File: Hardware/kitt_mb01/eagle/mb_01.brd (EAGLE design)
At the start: 160 x 100 mm, 120 parts, among them IC2.00 BQ24266RGET, IC3.01 LSM9DS1, U1.01 RT8293A, U6.01 TPS61032RSARPSDO-G16, U7.01 SI1922EDH, U7.03 SI1922EDH, U7.2 SI1922EDH, X2.01 S2B-PH-K-S(LF)(SN), X7.02 ARDUINO_UNO, X7.03 CON_HEADER_1X02, X7.05 MOTOR, X7.06 CON_HEADER_1X02, X7.08 CON_HEADER_1X02, X7.09 0R-JUMPA, X7.10 0R-JUMPA, X7.11 CON_HEADER_1X02

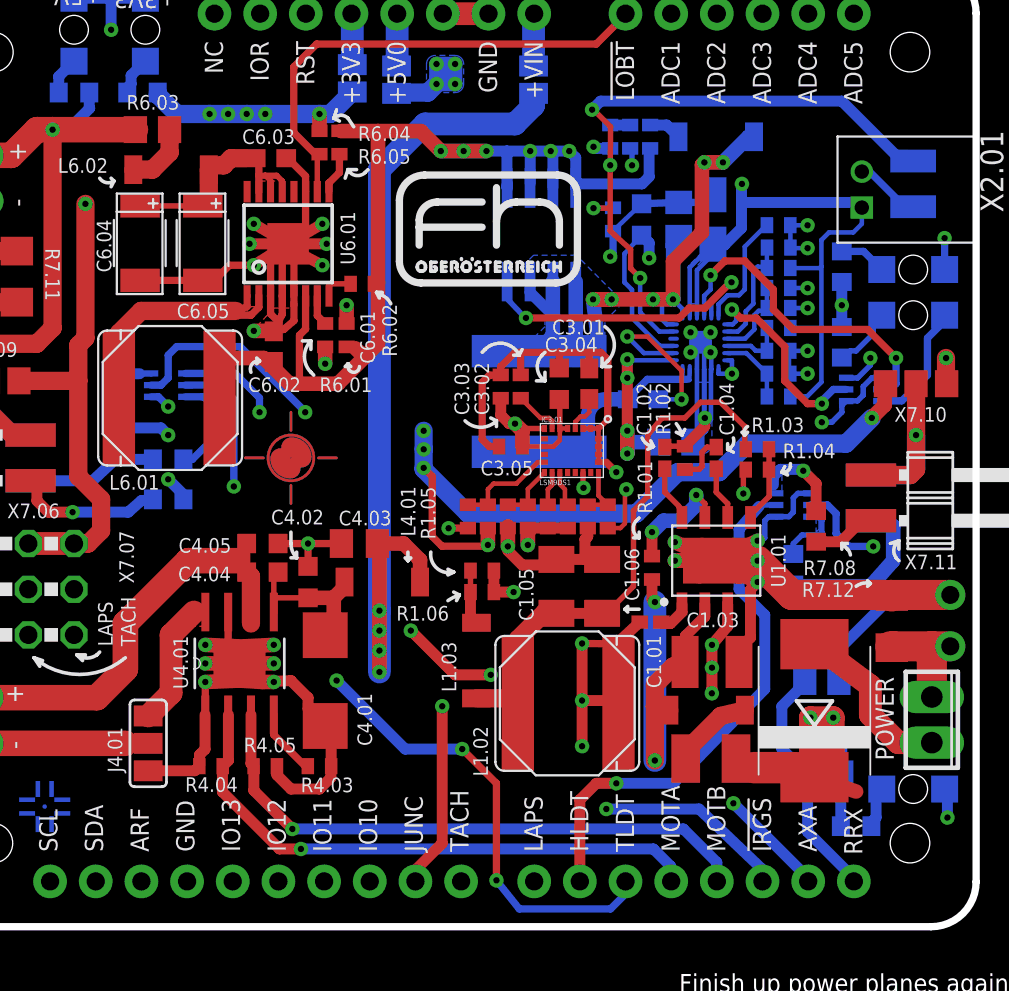
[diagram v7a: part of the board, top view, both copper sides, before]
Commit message: snapshot of mb01 board layout -> forgot a DRC check for the silk layer -> fixed all overlaps for top silk
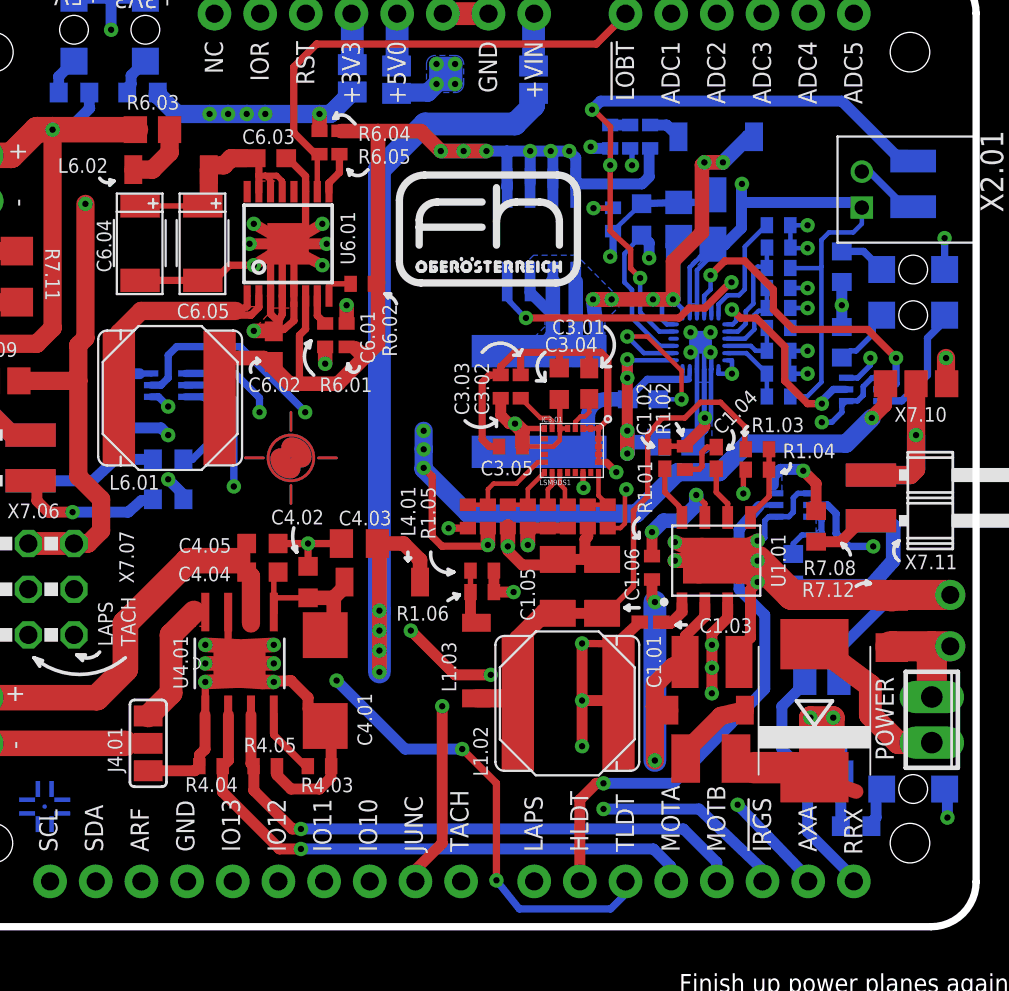
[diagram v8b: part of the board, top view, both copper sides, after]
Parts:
- moved C1.05 0.08 mm to (81.8, 39.5)
- renumbered FB2.01 to L2.02
